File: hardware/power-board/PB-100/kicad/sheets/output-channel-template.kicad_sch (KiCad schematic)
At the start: 0 parts

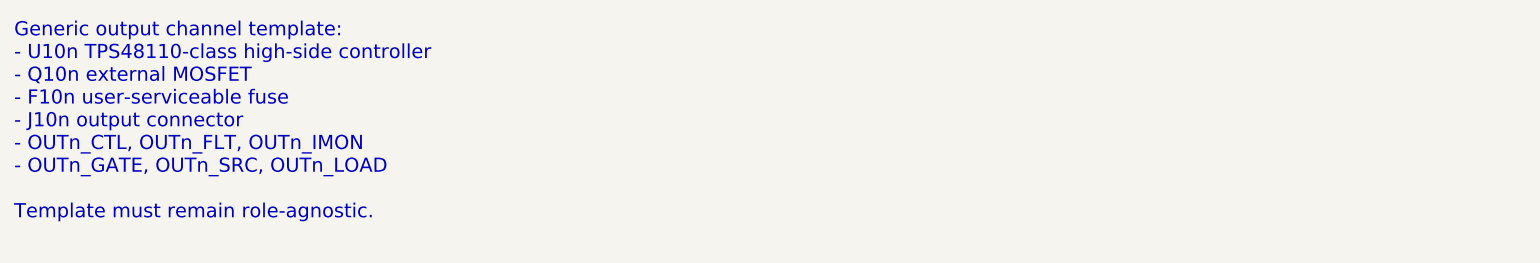
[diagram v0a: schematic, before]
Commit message: hardware: sync pb100 kicad sheet trace notes
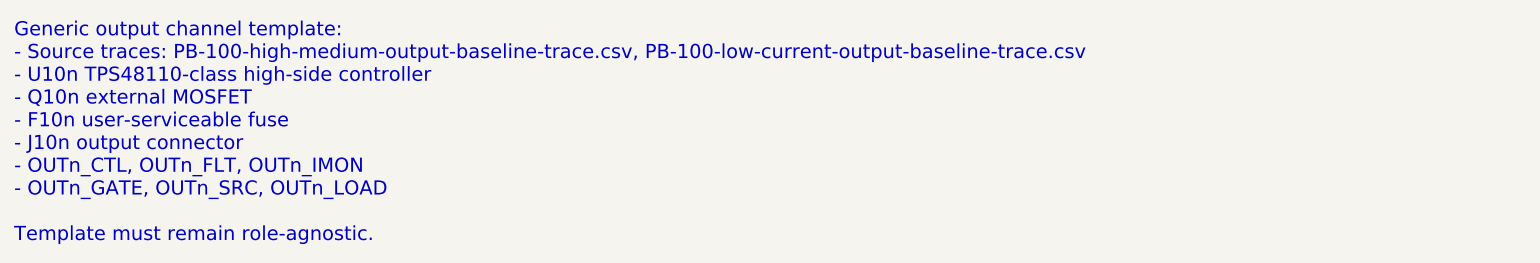
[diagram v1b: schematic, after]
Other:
- note added: "Generic output channel template: - Source traces: PB-100-high-medium-output-baseline-trace.csv, PB-100-low-current-output-baseline-trace.csv - U10n TPS48110-class high-side controller - Q10n external MOSFET - F10n user-serviceable fuse - J10n output connector - OUTn_CTL, OUTn_FLT, OUTn_IMON - OUTn_GATE, OUTn_SRC, OUTn_LOAD Template must remain role-agnostic."
- note removed: "Generic output channel template: - U10n TPS48110-class high-side controller - Q10n external MOSFET - F10n user-serviceable fuse - J10n output connector - OUTn_CTL, OUTn_FLT, OUTn_IMON - OUTn_GATE, OUTn_SRC, OUTn_LOAD Template must remain role-agnostic."
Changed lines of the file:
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@@
     (comment 9 "Work queue: CAP-OUT-TEMPLATE. Output template capture follows controller pin template.")
     (comment 1 "Placeholder sheet. Capture one generic TPS48110 + MOSFET output stage pattern here.")
-    (comment 2 "Use OUTn nets only. Do not encode accessory roles.")
+    (comment 2 "Sources: PB-100-high-medium-output-baseline-trace.csv and PB-100-low-current-output-baseline-trace.csv. Use OUTn nets only.")
   )
-  (text "Generic output channel template:\n- U10n TPS48110-class high-side controller\n- Q10n external MOSFET\n- F10n user-serviceable fuse\n- J10n output connector\n- OUTn_CTL, OUTn_FLT, OUTn_IMON\n- OUTn_GATE, OUTn_SRC, OUTn_LOAD\n\nTemplate must remain role-agnostic."
+  (text "Generic output channel template:\n- Source traces: PB-100-high-medium-output-baseline-trace.csv, PB-100-low-current-output-baseline-trace.csv\n- U10n TPS48110-class high-side controller\n- Q10n external MOSFET\n- F10n user-serviceable fuse\n- J10n output connector\n- OUTn_CTL, OUTn_FLT, OUTn_IMON\n- OUTn_GATE, OUTn_SRC, OUTn_LOAD\n\nTemplate must remain role-agnostic."
     (at 25 30 0)
     (effects (font (size 2.0 2.0)) (justify left top))

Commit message: hardware: add pb100 output stage freeze reviews
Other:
- note added: "Generic output channel template: - Source traces: PB-100-high-medium-output-baseline-trace.csv, PB-100-high-medium-output-freeze-review.csv, PB-100-low-current-output-baseline-trace.csv, PB-100-low-current-output-freeze-review.csv - U10n TPS48110-class high-side controller - Q10n external MOSFET - F10n user-serviceable fuse - J10n output connector - OUTn_CTL, OUTn_FLT, OUTn_IMON - OUTn_GATE, OUTn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"
- note removed: "Generic output channel template: - Source traces: PB-100-high-medium-output-baseline-trace.csv, PB-100-low-current-output-baseline-trace.csv - U10n TPS48110-class high-side controller - Q10n external MOSFET - F10n user-serviceable fuse - J10n output connector - OUTn_CTL, OUTn_FLT, OUTn_IMON - OUTn_GATE, OUTn_SRC, OUTn_LOAD Template must remain role-agnostic."
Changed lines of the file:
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@@
     (comment 9 "Work queue: CAP-OUT-TEMPLATE. Output template capture follows controller pin template.")
     (comment 1 "Placeholder sheet. Capture one generic TPS48110 + MOSFET output stage pattern here.")
-    (comment 2 "Sources: PB-100-high-medium-output-baseline-trace.csv and PB-100-low-current-output-baseline-trace.csv. Use OUTn nets only.")
+    (comment 2 "Sources: PB-100-high-medium-output-baseline-trace.csv, PB-100-high-medium-output-freeze-review.csv, PB-100-low-current-output-baseline-trace.csv, PB-100-low-current-output-freeze-review.csv. Use OUTn nets only.")
   )
-  (text "Generic output channel template:\n- Source traces: PB-100-high-medium-output-baseline-trace.csv, PB-100-low-current-output-baseline-trace.csv\n- U10n TPS48110-class high-side controller\n- Q10n external MOSFET\n- F10n user-serviceable fuse\n- J10n output connector\n- OUTn_CTL, OUTn_FLT, OUTn_IMON\n- OUTn_GATE, OUTn_SRC, OUTn_LOAD\n\nTemplate must remain role-agnostic."
+  (text "Generic output channel template:\n- Source traces: PB-100-high-medium-output-baseline-trace.csv, PB-100-high-medium-output-freeze-review.csv, PB-100-low-current-output-baseline-trace.csv, PB-100-low-current-output-freeze-review.csv\n- U10n TPS48110-class high-side controller\n- Q10n external MOSFET\n- F10n user-serviceable fuse\n- J10n output connector\n- OUTn_CTL, OUTn_FLT, OUTn_IMON\n- OUTn_GATE, OUTn_SRC, OUTn_LOAD\n- Gate drive, sense, threshold, timer, clamp, and no-smart-switch boundaries remain freeze-review items\n\nTemplate must remain role-agnostic."
     (at 25 30 0)
     (effects (font (size 2.0 2.0)) (justify left top))

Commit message: Capture preliminary PB-100 schematic sheets
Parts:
- added U100: OUTPUT_CHANNEL_PRELIM, symbol PB100:PB100_OUTPUT_CHANNEL_PRELIM
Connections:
- new net GND: U100.6 (GND)
- new net OUTn_CTL: U100.2 (OUTn_CTL)
- new net OUTn_FLT: U100.3 (OUTn_FLT)
- new net OUTn_IMON: U100.4 (OUTn_IMON)
- new net OUTn_LOAD: U100.5 (OUTn_LOAD)
- new net VBAT_PROT: U100.1 (VBAT_PROT)
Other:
- note added: "Output channel template capture notes: - Source traces: PB-100-high-medium-output-baseline-trace.csv, PB-100-high-medium-output-freeze-review.csv, PB-100-low-current-output-baseline-trace.csv, PB-100-low-current-output-freeze-review.csv - Template nets use OUTn_* only and remain role-agnostic - Threshold, timing, bootstrap, sense, and clamp values remain schematic-freeze work No PCB layout from t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"
- note removed: "Generic output channel template: - Source traces: PB-100-high-medium-output-baseline-trace.csv, PB-100-high-medium-output-freeze-review.csv, PB-100-low-current-output-baseline-trace.csv, PB-100-low-current-output-freeze-review.csv - U10n TPS48110-class high-side controller - Q10n external MOSFET - F10n user-serviceable fuse - J10n output connector - OUTn_CTL, OUTn_FLT, OUTn_IMON - OUTn_GATE, OUTn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"
- title: PB-100 Generic Output Channel Template -> PB-100 Output Channel Template
